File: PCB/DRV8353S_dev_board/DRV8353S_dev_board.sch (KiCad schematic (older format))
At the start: 141 parts, among them J1 HC_POWER, J2 MOT_LC, J3 SWD, J4 EXT_CMD, J5 PHASE, Q1 BSS84, Q2 CSD19502, Q3 CSD19502, Q4 CSD19502, Q5 CSD19502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

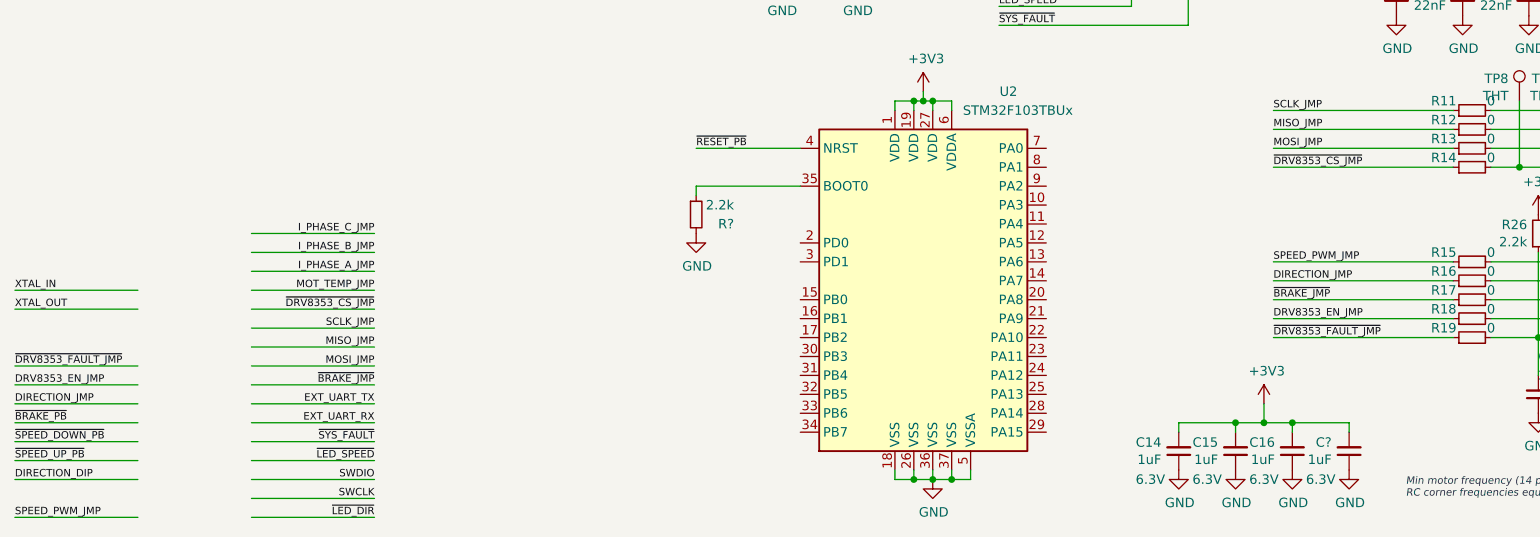
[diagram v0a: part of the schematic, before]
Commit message: updated MCU due to low digi stock. This was bad routing to get new MCU pinout
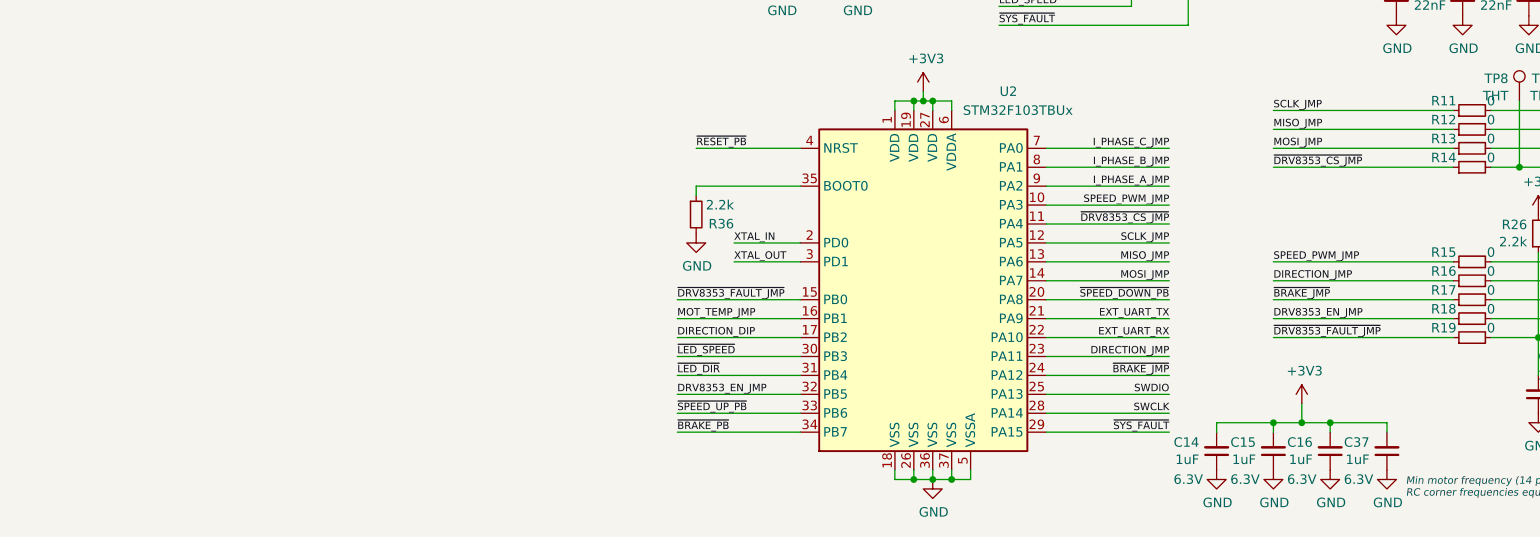
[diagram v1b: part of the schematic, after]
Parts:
- gave numbers to parts that had none: 2
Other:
- moved on the sheet: C14, C15, C16, C37

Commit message: Good routing
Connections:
- net DRV8353_EN_JMP: now also U2.34 (PB7); no longer U2.32 (PB5)
- net ~BRAKE_PB: now also U2.32 (PB5); no longer U2.34 (PB7)
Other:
- note added: "- Voltage: 25V - 50V\n- Max Current: 100A\n- Cont. Current: 50A\n- Sensored 120 deg commutation \n- For use with Flipsky 6384"
- note removed: "- Voltage: 25V - 50V\n- Max Current: 100A\n- Cont. Current: 50A\n- Sensored 120 deg trap. commutation \n- For use with Flipsky 6384"
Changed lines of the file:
@@
 DRV8353SM Dev. Board
 Text Notes 4200 1300 0    50   Italic 0
-- Voltage: 25V - 50V\n- Max Current: 100A\n- Cont. Current: 50A\n- Sensored 120 deg trap. commutation \n- For use with Flipsky 6384
+- Voltage: 25V - 50V\n- Max Current: 100A\n- Cont. Current: 50A\n- Sensored 120 deg commutation \n- For use with Flipsky 6384
 Text Notes 5900 1150 0    50   Italic 0
 Evaluation prototype for\nopen source e-mobility\nplatform.
@@
 Text Label 3150 5800 2    39   ~ 0
 I_PHASE_C_JMP
-Text Label 550  7100 0    39   ~ 0
+Text Label 550  7300 0    39   ~ 0
 DRV8353_EN_JMP
 Wire Wire Line
@@
 	2500 6700 3150 6700
 Wire Wire Line
-	1200 7100 550  7100
+	1200 7300 550  7300
 Wire Wire Line
 	2500 6500 3150 6500
@@
 Text Label 3150 6600 2    39   ~ 0
 ~SPEED_DOWN_PB
-Text Label 550  7300 0    39   ~ 0
+Text Label 550  7100 0    39   ~ 0
 ~BRAKE_PB
 Text Label 3150 7300 2    39   ~ 0
@@
 	3150 6600 2500 6600
 Wire Wire Line
-	550  7300 1200 7300
+	550  7100 1200 7100
 $Comp
 L DRV8353S_dev_board-rescue:+3V3-power #PWR?
